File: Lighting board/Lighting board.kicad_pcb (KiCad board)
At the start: 2 copper layers, 16 parts, among them SW1 SW_SPDT, U1 LDD-1500L, U2 LDD-1500L, U3 TM4C129E_Launchpad, U4 OKI

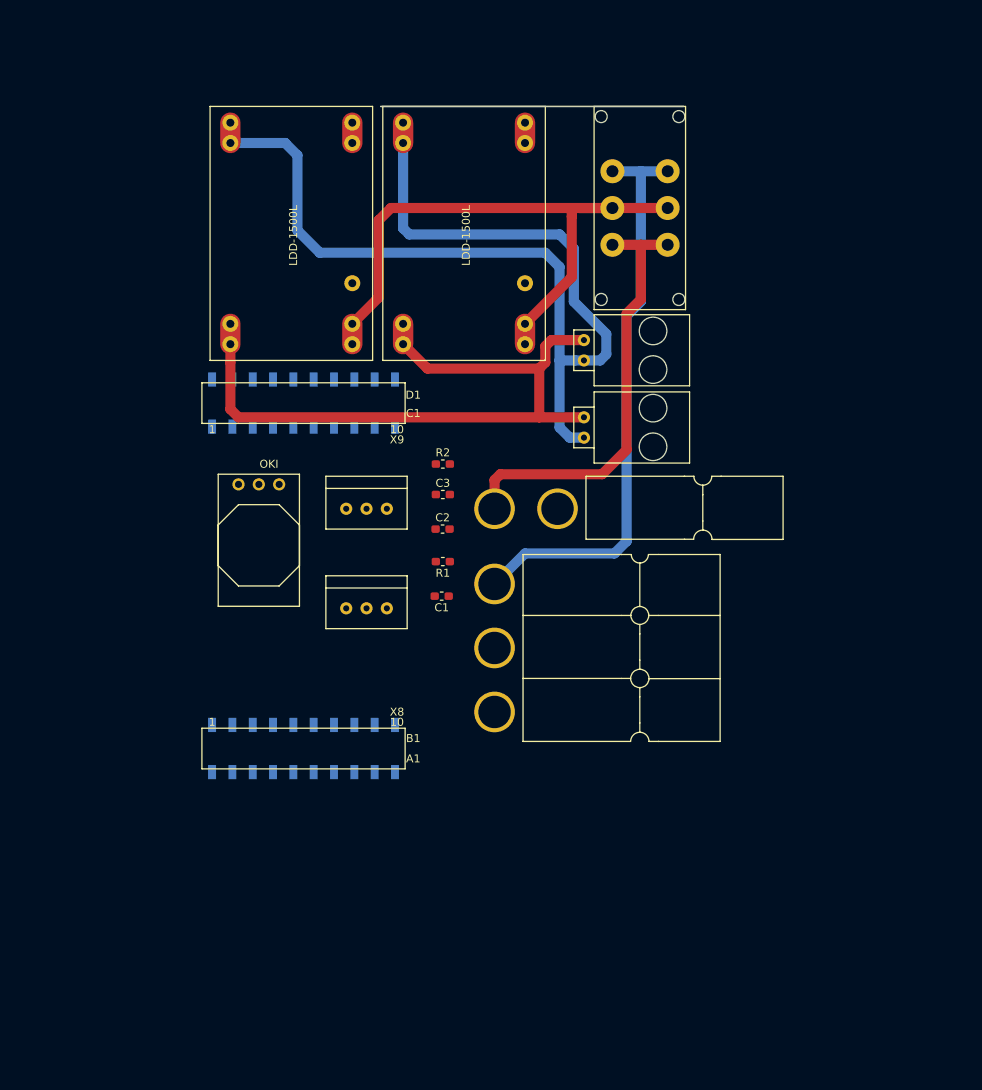
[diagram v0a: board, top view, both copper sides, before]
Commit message: Changes 11/3
changed oki to AP1059 and started traces
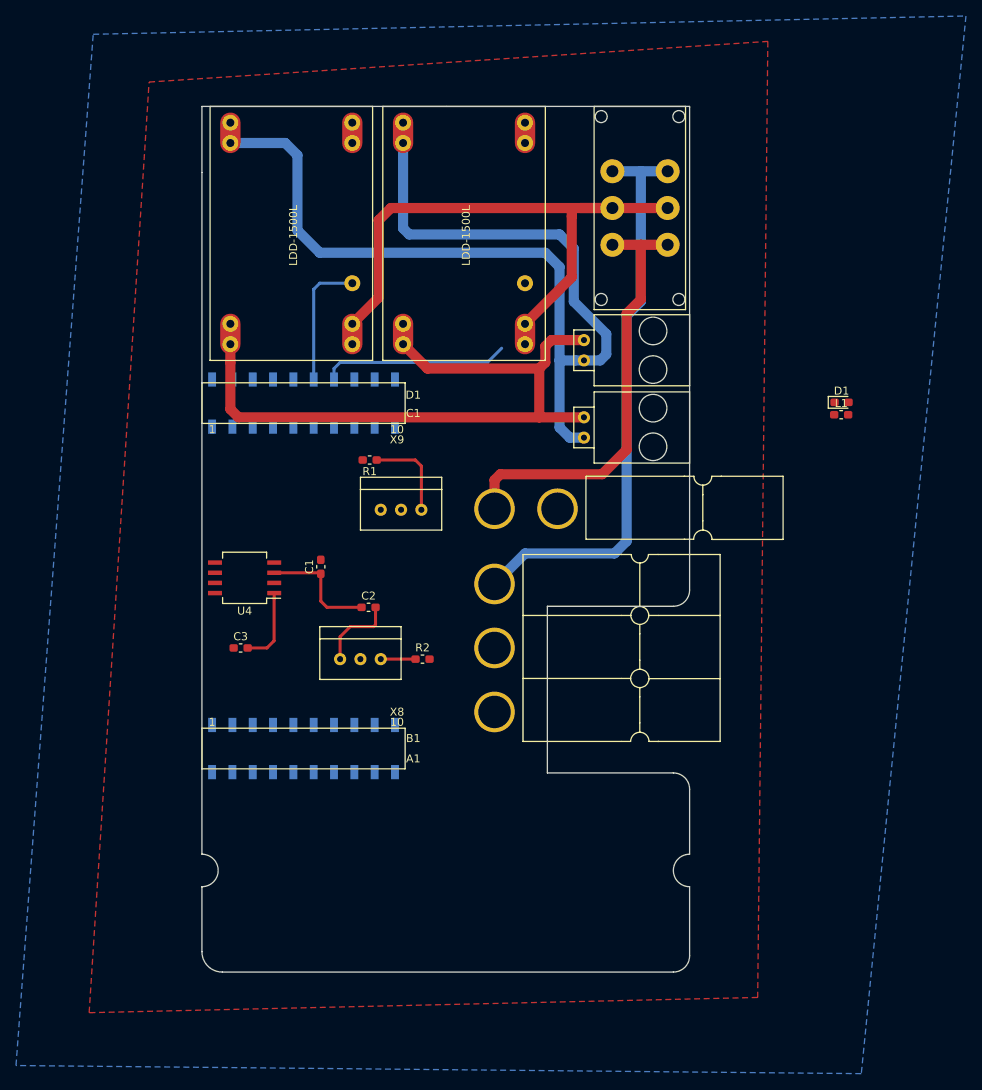
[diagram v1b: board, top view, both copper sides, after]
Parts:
- added D1: D_Schottky, Diode_SMD:D_0603_1608Metric_Pad1.05x0.95mm_HandSolder, F.Cu at (162.8, 98.5)
- added L1: 47uH, Inductor_SMD:L_0603_1608Metric_Pad1.05x0.95mm_HandSolder, F.Cu at (162.7, 100.0)
- U4: value OKI -> AP1059; footprint MRDT_Devices:OKI_Horizontal -> Package_SO:SO-8_5.3x6.2mm_P1.27mm
- moved C3 31.7 mm to (87.6, 129.2)
- moved R2 24.5 mm to (110.4, 130.6)
- moved R1 15.6 mm to (103.8, 105.7)
- moved C1 15.6 mm to (97.7, 119.0), turned to 90 degrees
- moved C2 13.5 mm to (103.6, 124.1)
- moved U4 13.4 mm to (88.1, 120.4), turned to 180 degrees
- moved Conn2C2 6.40 mm to (97.5, 128.0)
- moved Conn2C1 4.32 mm to (102.6, 109.3)
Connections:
- net Dout_NeoPxiel2 renamed Net-(U3-PadPE4)
- C2 pad 2: Net-(C2-Pad2) -> GND
- C3 pad 1: /+12V -> GND
- C3 pad 2: Net-(C3-Pad2) -> /+12V
- Conn1 pad 1: Net-(C3-Pad2) -> GND
- Conn2 pad 4: PV+ -> (no net)
- U3 pad PD0: Headlight_OnOff_PWM2 -> Headlight_OnOff_PWM1
- U3 pad PD1: Headlight_OnOff_PWM1 -> Headlight_OnOff_PWM2
- U4 pad 2: Net-(C3-Pad2) -> Net-(D1-Pad1)
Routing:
- net Headlight_OnOff_PWM1: track 0.00 -> 23.4 mm
- net Headlight_OnOff_PWM2: track 0.00 -> 16.4 mm
- net 5V: track 0.00 -> 14.7 mm
- net Net-(Conn2C1-Pad3): track 0.00 -> 11.4 mm
- net Net-(C2-Pad2): track 0.00 -> 10.0 mm
- net /+12V: track 0.00 -> 9.65 mm
- net Net-(Conn2C2-Pad3): track 0.00 -> 4.35 mm
- added copper zone on B.Cu, net GND
- added copper zone on F.Cu, net GND
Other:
- board outline added: 61 x 108.2 mm
- rule trace_min: 0.2 -> 0.0381
- rule via_min_size: 0.4 -> 0.04
